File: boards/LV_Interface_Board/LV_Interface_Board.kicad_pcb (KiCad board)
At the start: 2 copper layers, 0 parts

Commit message: working on LV interface layout, added measurements to LV box boards to accurately place connectors
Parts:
- added C1: C_10uF, footprints:C_0805_OEM, F.Cu at (210.6, 129.2)
- added D1: D_Schottky_SOD123, footprints:D_SOD-123W_OEM, F.Cu at (180.8, 130.1)
- added D2: D_Schottky_SOD123, footprints:D_SOD-123W_OEM, F.Cu at (180.8, 124.1)
- added D3: D_Schottky_SOD123, footprints:D_SOD-123W_OEM, F.Cu at (192.9, 131.2)
- added D4: LED_0805, footprints:LED_0805_OEM, F.Cu at (203.4, 129.2)
- added F1: fuse_holder_125V_15A, footprints:fuse_block, F.Cu at (83.1, 143.9)
- added J1: Ampseal_35, footprints:Ampseal_35, F.Cu at (152.2, 51.5)
- added J2: Ampseal_35, footprints:Ampseal_35, F.Cu at (44.6, 54.0)
- added J3: micromatch_male_6, footprints:micromatch_female_ra_6, F.Cu at (76.5, 113.4)
- added J4: micromatch_male_20, footprints:micromatch_female_ra_20, F.Cu at (108.5, 113.4)
- added J5: micromatch_male_20, footprints:micromatch_female_ra_20, F.Cu at (109.0, 86.6)
- added J6: micromatch_male_12, footprints:micromatch_female_ra_12, F.Cu at (112.0, 101.3)
- added J7: micromatch_male_18, footprints:micromatch_female_ra_18, F.Cu at (89.9, 101.6)
- added J8: micromatch_male_20, footprints:micromatch_female_ra_20, F.Cu at (104.7, 63.0)
- added J9: micromatch_male_20, footprints:micromatch_female_ra_20, F.Cu at (98.0, 77.8)
- added LED1: SEGMENT_12BAR_BICOLOR, footprints:SEGMENT_BICOL_BL-AR12Z3010, F.Cu at (49.5, 145.1)
- added LED2: SEGMENT_12BAR_BICOLOR, footprints:SEGMENT_BICOL_BL-AR12Z3010, F.Cu at (50.6, 130.4)
- added R1: R_500, footprints:R_0805_OEM, F.Cu at (184.5, 108.1)
- added R2: R_10k, footprints:R_0805_OEM, F.Cu at (189.3, 108.1)
- added R3: R_10k, footprints:R_0805_OEM, F.Cu at (184.4, 113.4)
- added SW1: 3P4T_rotary_switch, footprints:3P4T_rotary_switch, F.Cu at (122.4, 135.3)
- added U1: RJ45_VT, footprints:RJ45-Vertical, F.Cu at (147.8, 138.1)
- added U2: HT16K33, footprints:SOP28, F.Cu at (43.3, 164.7)

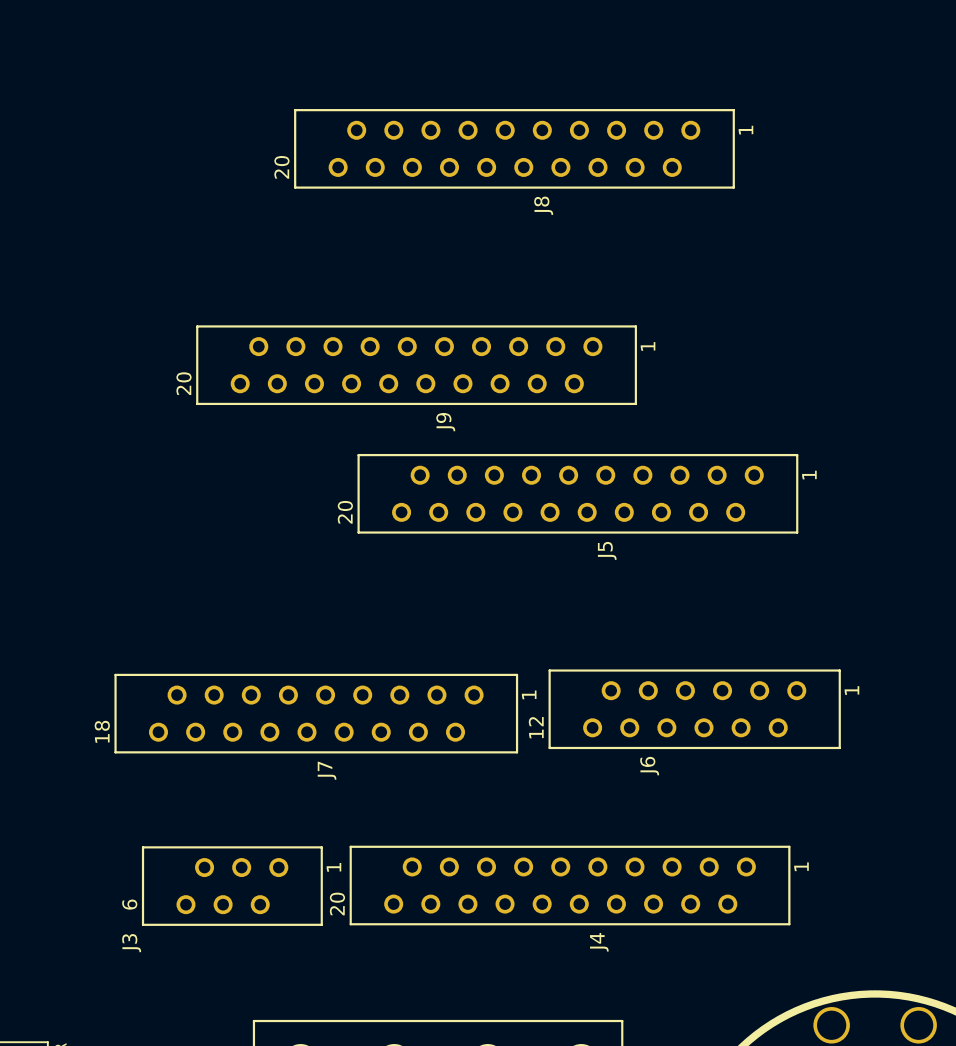
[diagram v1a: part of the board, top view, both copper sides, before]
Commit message: finalized micromatch locations
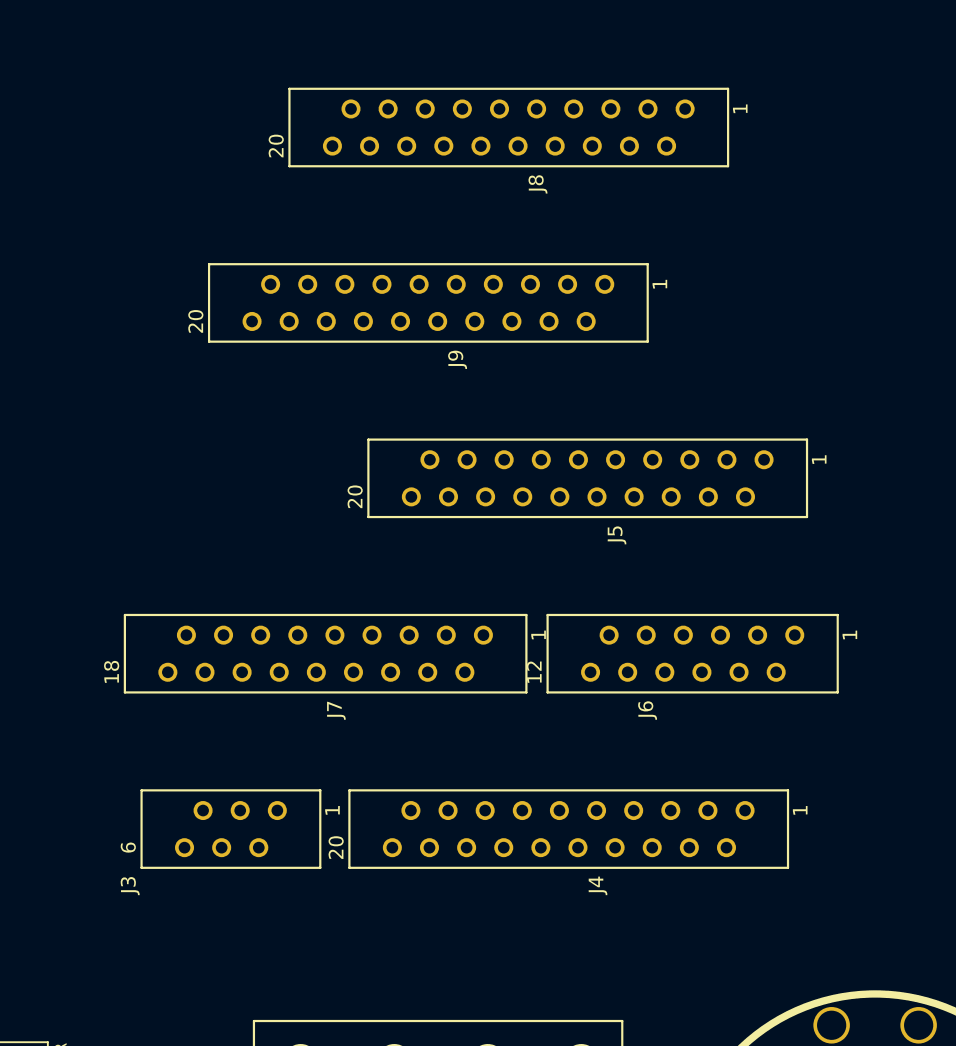
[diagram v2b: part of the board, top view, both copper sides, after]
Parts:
- moved J9 4.34 mm to (98.8, 73.5)
- moved J7 4.15 mm to (90.5, 97.5)
- moved J3 3.90 mm to (76.4, 109.5)
- moved J4 3.86 mm to (108.4, 109.5)
- moved J6 3.80 mm to (111.8, 97.5)
- moved J8 1.51 mm to (104.3, 61.5)
- moved J5 1.25 mm to (109.7, 85.5)
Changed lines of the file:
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@@
     (links 173)
     (no_connects 173)
-    (area 148.844 55.88 287.034991 135.964802)
+    (area 31.8124 42.3 213.457372 167.5986)
     (thickness 1.6)
-    (drawings 13)
+    (drawings 18)
     (tracks 0)
     (zones 0)
@@
   )
   (module footprints:micromatch_female_ra_6 (layer F.Cu)
-    (at 76.52 113.4 270)
+    (at 76.42 109.5 270)
     (fp_text reference J3 (at 5.08 5.08 270) (layer F.SilkS)
       (effects (font (size 1 1) (thickness 0.15)))
@@
   )
   (module footprints:micromatch_female_ra_20 (layer F.Cu)
-    (at 108.51 113.36 270)
+    (at 108.42 109.5 270)
     (fp_text reference J4 (at 5.08 5.08 270) (layer F.SilkS)
       (effects (font (size 1 1) (thickness 0.15)))
@@
   )
   (module footprints:micromatch_female_ra_20 (layer F.Cu)
-    (at 109.05 86.56 270)
+    (at 109.72 85.5 270)
     (fp_text reference J5 (at 5.08 5.08 270) (layer F.SilkS)
       (effects (font (size 1 1) (thickness 0.15)))
@@
   )
   (module footprints:micromatch_female_ra_12 (layer F.Cu)
-    (at 111.96 101.3 270)
+    (at 111.82 97.5 270)
     (fp_text reference J6 (at 5.08 5.08 270) (layer F.SilkS)
       (effects (font (size 1 1) (thickness 0.15)))
@@
   )
   (module footprints:micromatch_female_ra_18 (layer F.Cu)
-    (at 89.88 101.6 270)
+    (at 90.52 97.5 270)
     (fp_text reference J7 (at 5.08 5.08 270) (layer F.SilkS)
       (effects (font (size 1 1) (thickness 0.15)))
@@
   )
   (module footprints:micromatch_female_ra_20 (layer F.Cu)
-    (at 104.71 62.96 270)
+    (at 104.32 61.5 270)
     (fp_text reference J8 (at 5.08 5.08 270) (layer F.SilkS)
       (effects (font (size 1 1) (thickness 0.15)))
@@
   )
   (module footprints:micromatch_female_ra_20 (layer F.Cu)
-    (at 98.01 77.76 270)
+    (at 98.82 73.5 270)
     (fp_text reference J9 (at 5.08 5.08 270) (layer F.SilkS)
       (effects (font (size 1 1) (thickness 0.15)))
@@
       (net 93 /COM0))
   )
+  (dimension 2 (width 0.3) (layer Dwgs.User)
+    (gr_text "2.000 mm" (at 109.650001 107 270) (layer Dwgs.User)
+      (effects (font (size 1.5 1.5) (thickness 0.3)))
+    )
+    (feature1 (pts (xy 113 108) (xy 108.300001 108)))
+    (feature2 (pts (xy 113 106) (xy 108.300001 106)))
+    (crossbar (pts (xy 111.000001 106) (xy 111.000001 108)))
+    (arrow1a (pts (xy 111.000001 108) (xy 110.41358 106.873496)))
+    (arrow1b (pts (xy 111.000001 108) (xy 111.586422 106.873496)))
+    (arrow2a (pts (xy 111.000001 106) (xy 110.41358 107.126504)))
+    (arrow2b (pts (xy 111.000001 106) (xy 111.586422 107.126504)))
+  )
+  (dimension 2 (width 0.3) (layer Dwgs.User)
+    (gr_text "2.000 mm" (at 112.650001 95 270) (layer Dwgs.User)
+      (effects (font (size 1.5 1.5) (thickness 0.3)))
+    )
+    (feature1 (pts (xy 116 96) (xy 111.300001 96)))
+    (feature2 (pts (xy 116 94) (xy 111.300001 94)))
+    (crossbar (pts (xy 114.000001 94) (xy 114.000001 96)))
+    (arrow1a (pts (xy 114.000001 96) (xy 113.41358 94.873496)))
+    (arrow1b (pts (xy 114.000001 96) (xy 114.586422 94.873496)))
+    (arrow2a (pts (xy 114.000001 94) (xy 113.41358 95.126504)))
+    (arrow2b (pts (xy 114.000001 94) (xy 114.586422 95.126504)))
+  )
+  (dimension 2 (width 0.3) (layer Dwgs.User)
+    (gr_text "2.000 mm" (at 111.65 83 270) (layer Dwgs.User)
+      (effects (font (size 1.5 1.5) (thickness 0.3)))
+    )
+    (feature1 (pts (xy 115 84) (xy 110.3 84)))
+    (feature2 (pts (xy 115 82) (xy 110.3 82)))
+    (crossbar (pts (xy 113 82) (xy 113 84)))
+    (arrow1a (pts (xy 113 84) (xy 112.413579 82.873496)))
+    (arrow1b (pts (xy 113 84) (xy 113.586421 82.873496)))
+    (arrow2a (pts (xy 113 82) (xy 112.413579 83.126504)))
+    (arrow2b (pts (xy 113 82) (xy 113.586421 83.126504)))
+  )
+  (dimension 2 (width 0.3) (layer Dwgs.User)
+    (gr_text "2.000 mm" (at 95.65 71 270) (layer Dwgs.User)
+      (effects (font (size 1.5 1.5) (thickness 0.3)))
+    )
+    (feature1 (pts (xy 100 72) (xy 94.3 72)))
+    (feature2 (pts (xy 100 70) (xy 94.3 70)))
+    (crossbar (pts (xy 97 70) (xy 97 72)))
+    (arrow1a (pts (xy 97 72) (xy 96.413579 70.873496)))
+    (arrow1b (pts (xy 97 72) (xy 97.586421 70.873496)))
+    (arrow2a (pts (xy 97 70) (xy 96.413579 71.126504)))
+    (arrow2b (pts (xy 97 70) (xy 97.586421 71.126504)))
+  )
+  (dimension 10 (width 0.3) (layer Dwgs.User)
+    (gr_text "10.000 mm" (at 103.650001 55 270) (layer Dwgs.User)
+      (effects (font (size 1.5 1.5) (thickness 0.3)))
+    )
+    (feature1 (pts (xy 110 60) (xy 102.300001 60)))
+    (feature2 (pts (xy 110 50) (xy 102.300001 50)))
+    (crossbar (pts (xy 105.000001 50) (xy 105.000001 60)))
+    (arrow1a (pts (xy 105.000001 60) (xy 104.41358 58.873496)))
+    (arrow1b (pts (xy 105.000001 60) (xy 105.586422 58.873496)))
+    (arrow2a (pts (xy 105.000001 50) (xy 104.41358 51.126504)))
+    (arrow2b (pts (xy 105.000001 50) (xy 105.586422 51.126504)))
+  )
   (dimension 45.5 (width 0.3) (layer Dwgs.User)

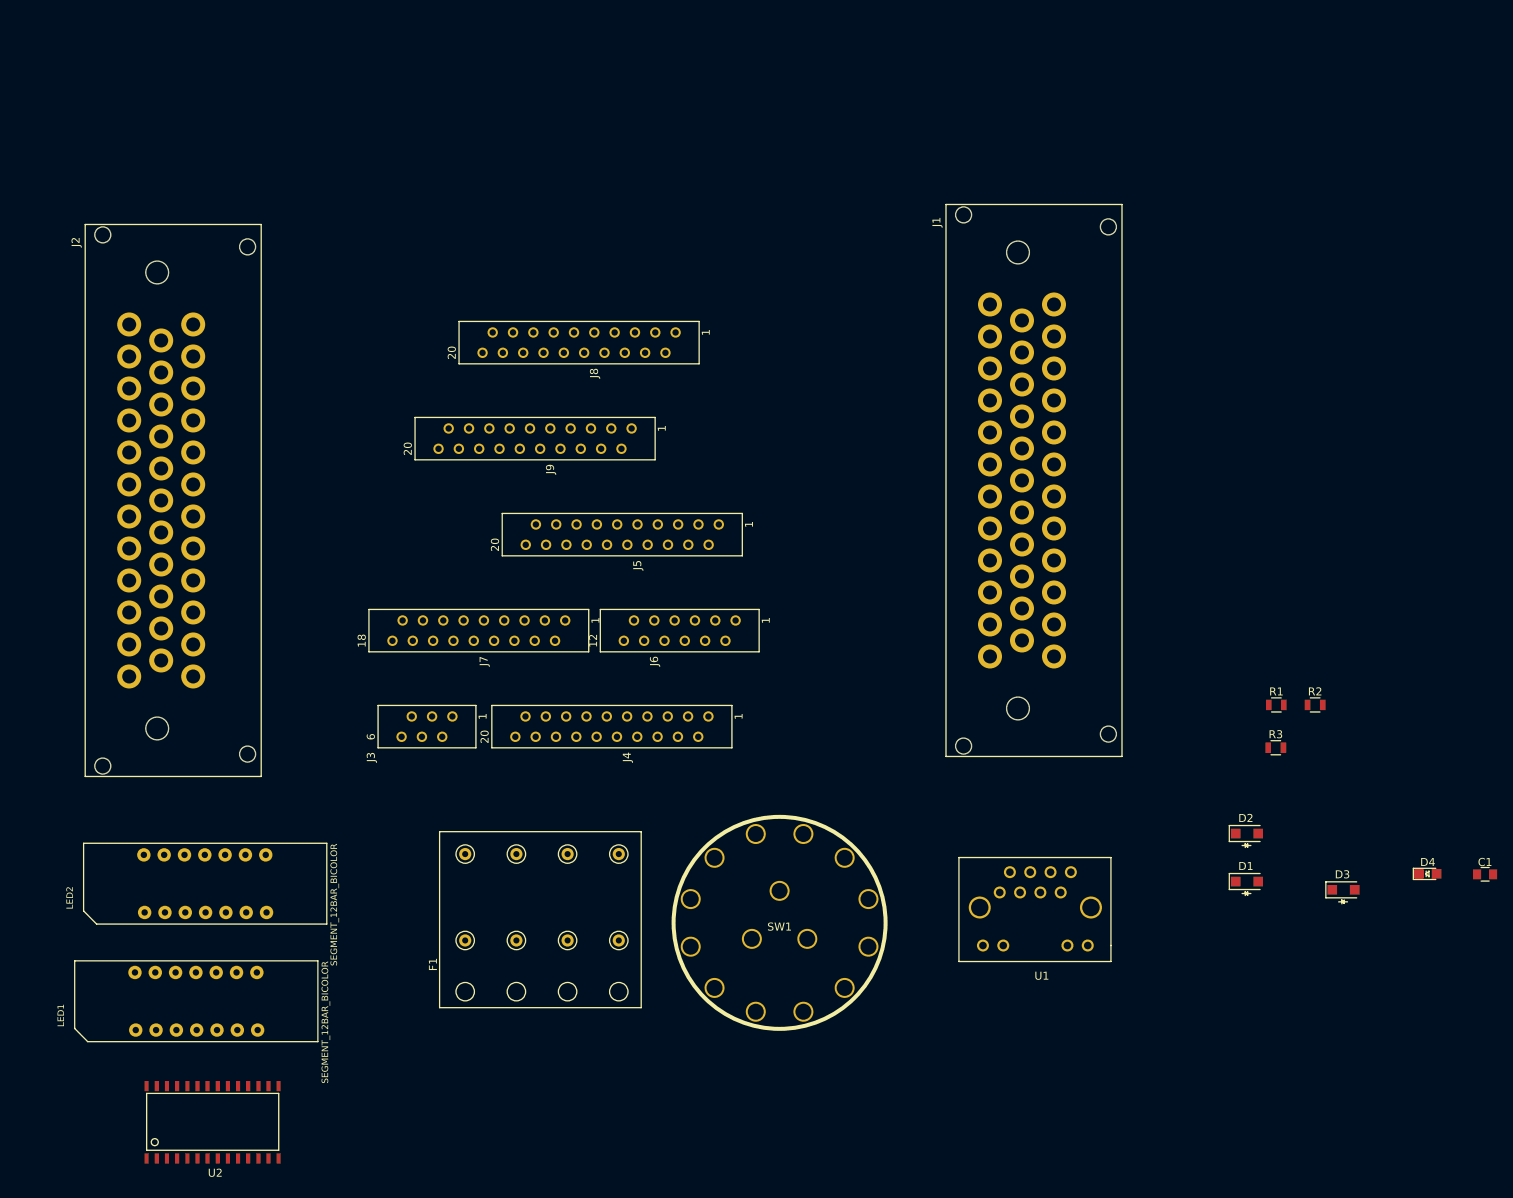
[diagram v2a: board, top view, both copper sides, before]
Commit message: finished layout for lv interface, adding CAD now and switching to ubuntu to export board CAD for mechanical
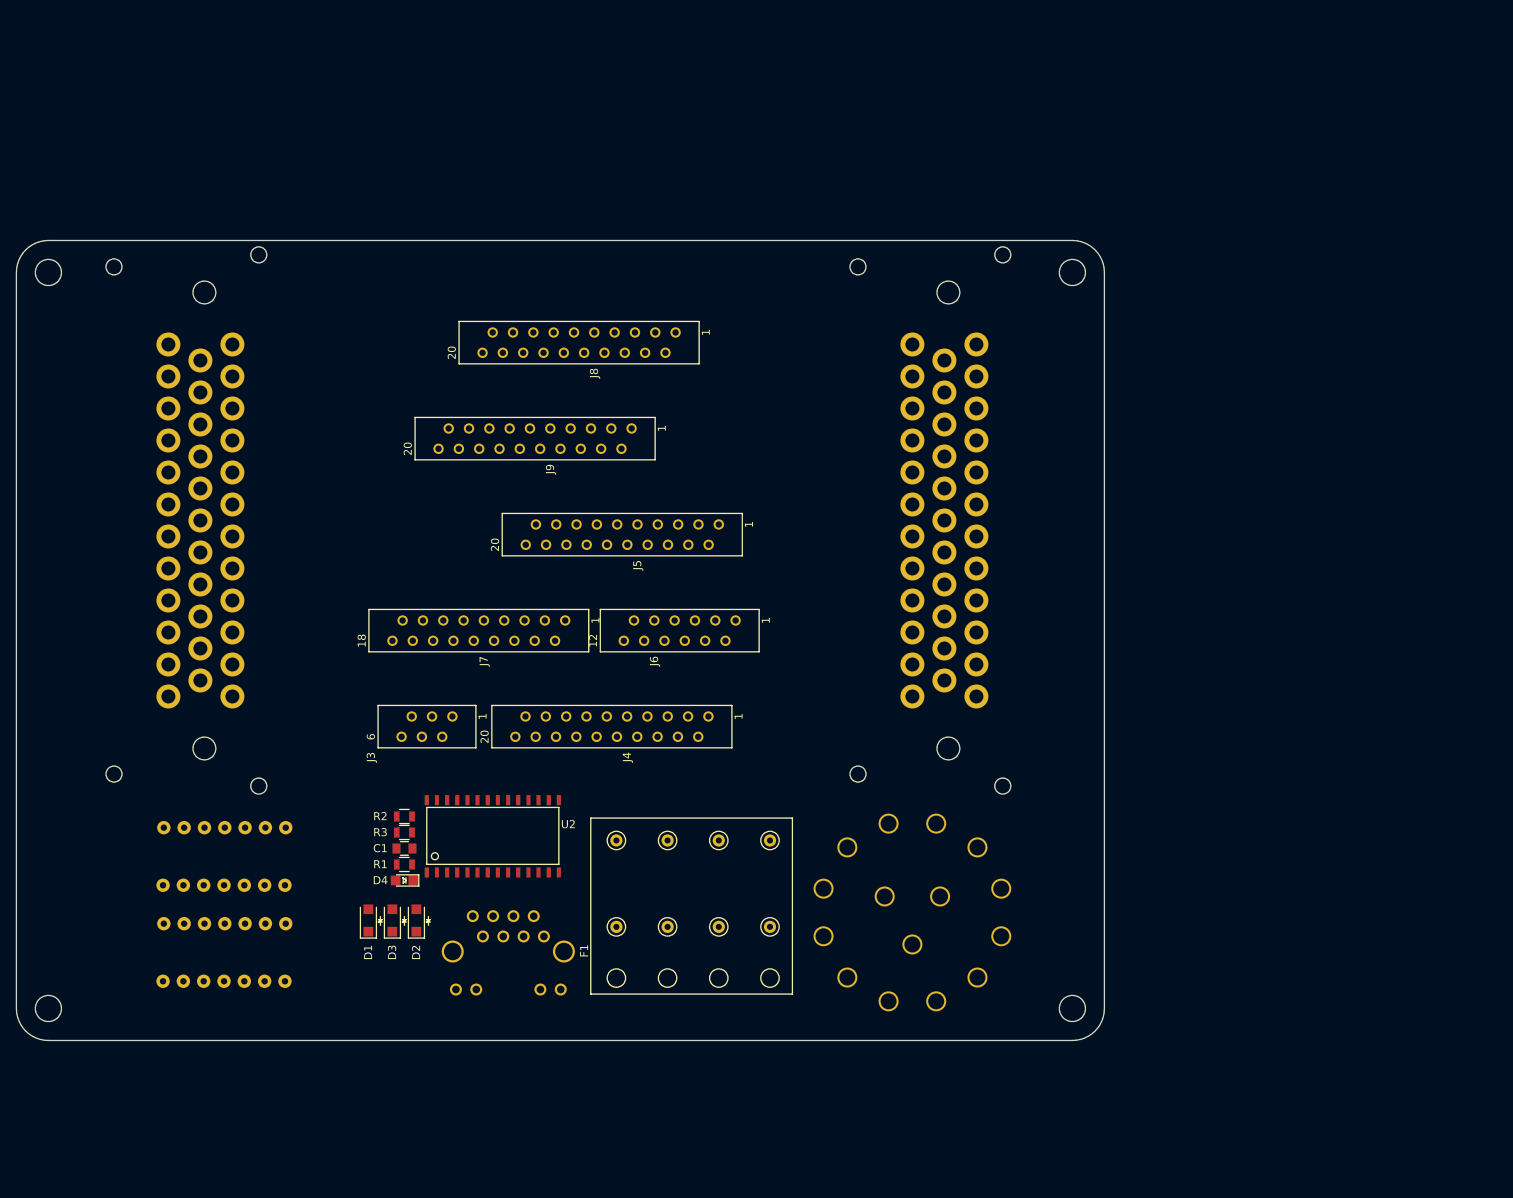
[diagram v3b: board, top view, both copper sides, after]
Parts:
- J1, J2, LED1, LED2, SW1, U1: moved to B.Cu
- moved C1 135.1 mm to (75.5, 126.0)
- moved D4 127.9 mm to (75.5, 130.0), turned to 180 degrees
- moved D3 118.9 mm to (74.0, 135.0), turned to 90 degrees
- moved R2 114.7 mm to (75.5, 122.0)
- moved R1 110.8 mm to (75.5, 128.0)
- moved D1 109.9 mm to (71.0, 135.0), turned to 90 degrees
- moved R3 109.4 mm to (75.5, 124.0)
- moved D2 104.4 mm to (77.0, 135.0), turned to 90 degrees
- moved U1 53.1 mm to (95.0, 143.6), turned to 180 degrees
- moved U2 50.0 mm to (78.3, 129.0)
- moved F1 19.0 mm to (102.0, 142.2)
- moved SW1 16.7 mm to (139.0, 134.0)
- moved J1 10.0 mm to (143.5, 56.5)
- moved LED1 7.04 mm to (53.0, 139.0), turned to 270 degrees
- moved J2 6.41 mm to (50.5, 56.5)
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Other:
- board outline added: 136 x 100 mm
